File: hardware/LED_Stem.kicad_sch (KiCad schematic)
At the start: 4 parts

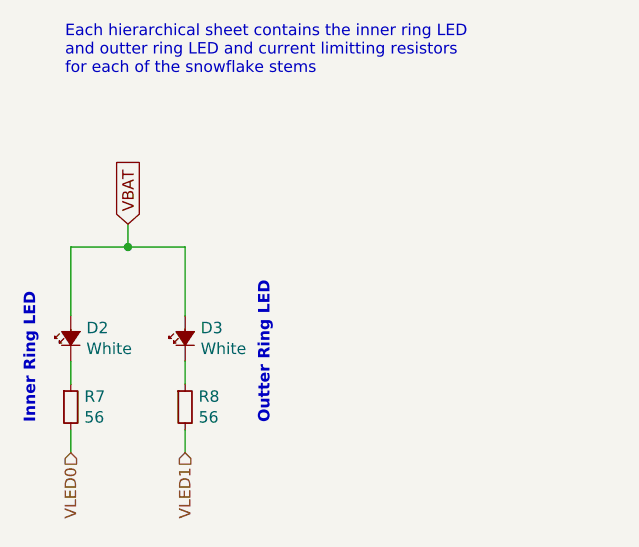
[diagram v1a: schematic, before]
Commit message: Changed the Counter footprint to 16-SOIC
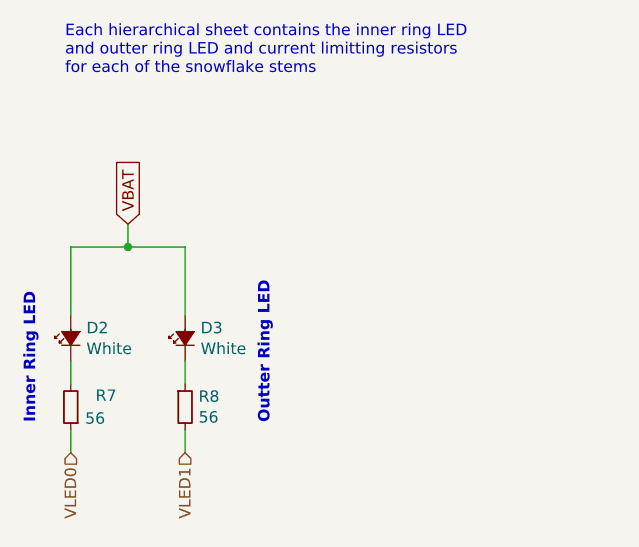
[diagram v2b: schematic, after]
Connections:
- net VLED0: now also R7.1; no longer R7.2
- net at D2.K: now also R7.2; no longer R7.1
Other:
- moved on the sheet: R7
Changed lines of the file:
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@@
     )
   )
-  (symbol (lib_id "Snowflake:R_Small") (at 50.8 73.66 0) (unit 1)
+  (symbol (lib_id "Snowflake:R_Small") (at 50.8 73.66 180) (unit 1)
     (in_bom yes) (on_board yes) (dnp no)
-    (property "Reference" "R7" (at 52.2986 72.4916 0)
+    (property "Reference" "R7" (at 55.88 72.39 0)
       (effects (font (size 1.27 1.27)) (justify left))
     )
-    (property "Value" "56" (at 52.2986 74.803 0)
+    (property "Value" "56" (at 54.61 74.93 0)
       (effects (font (size 1.27 1.27)) (justify left))
     )

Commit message: Added some stuff missing from the BoM Changed the LED component name from 4014 to 3014 (typo). Updated schematic and board
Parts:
- D2, D3: footprint Snowflake:4014_LED_HandSolder_NoSilk -> Snowflake:3014_LED_HandSolder_NoSilk
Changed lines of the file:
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@@
       (effects (font (size 1.27 1.27)) (justify right))
     )
-    (property "Footprint" "Snowflake:4014_LED_HandSolder_NoSilk" (at 50.8 66.04 90)
+    (property "Footprint" "Snowflake:3014_LED_HandSolder_NoSilk" (at 50.8 66.04 90)
       (effects (font (size 1.27 1.27)) hide)
     )
-    (property "Datasheet" "~" (at 50.8 66.04 90)
+    (property "Datasheet" "https://dammedia.osram.info/media/resource/hires/osram-dam-16984996/KW%20DCLMS2.EC_EN.pdf" (at 50.8 66.04 90)
       (effects (font (size 1.27 1.27)) hide)
     )
@@
       (effects (font (size 1.27 1.27)) (justify right))
     )
-    (property "Footprint" "Snowflake:4014_LED_HandSolder_NoSilk" (at 63.5 66.04 90)
+    (property "Footprint" "Snowflake:3014_LED_HandSolder_NoSilk" (at 63.5 66.04 90)
       (effects (font (size 1.27 1.27)) hide)
     )
-    (property "Datasheet" "~" (at 63.5 66.04 90)
+    (property "Datasheet" "https://dammedia.osram.info/media/resource/hires/osram-dam-16984996/KW%20DCLMS2.EC_EN.pdf" (at 63.5 66.04 90)
       (effects (font (size 1.27 1.27)) hide)
     )
